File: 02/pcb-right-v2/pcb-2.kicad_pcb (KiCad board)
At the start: 2 copper layers, 146.9 x 86 mm, 44 parts, among them U1 Arduino_Pro_Micro, U2 TRRS

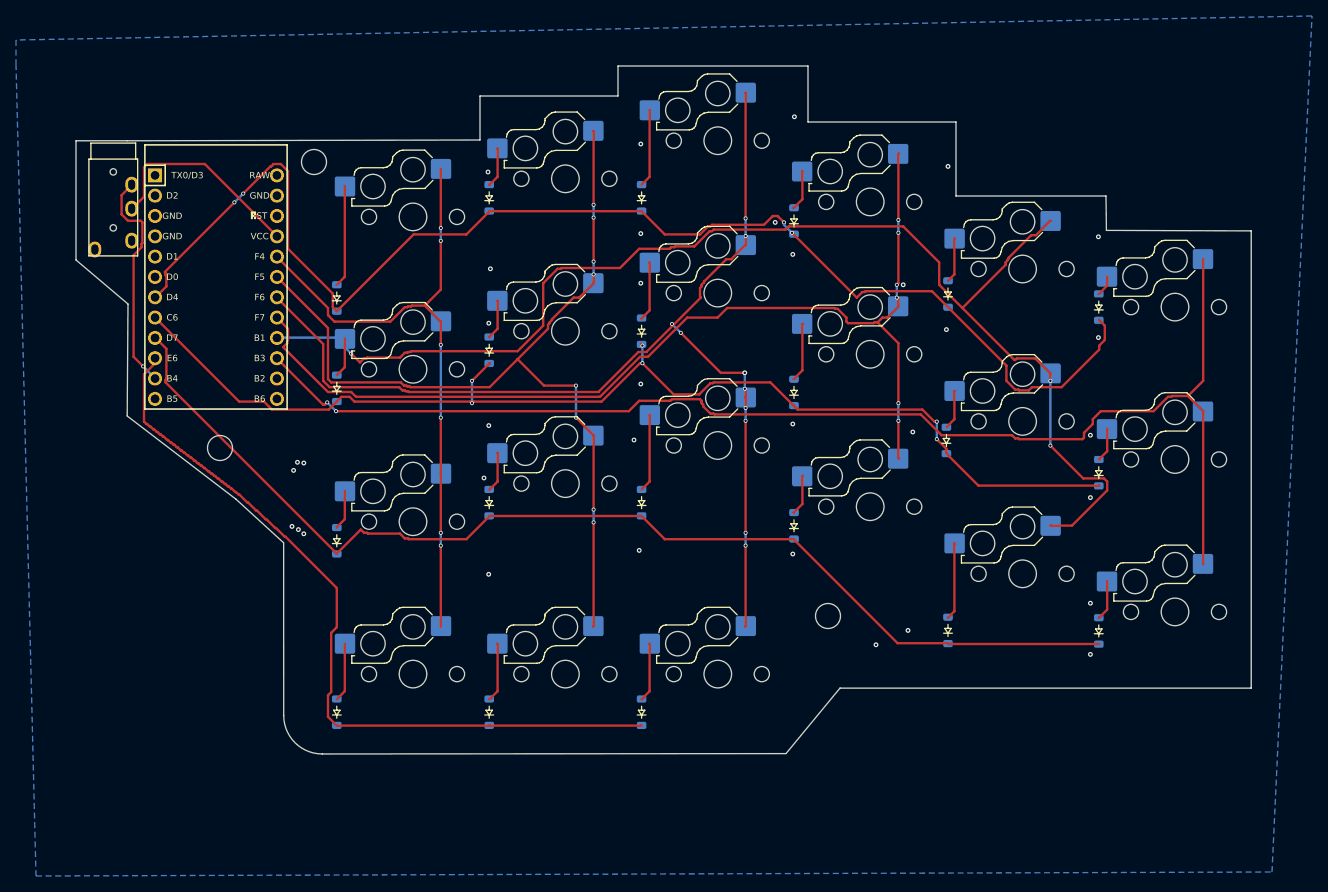
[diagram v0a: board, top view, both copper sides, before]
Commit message: fix: pcb-right-v2 switch/TRRS/MCU footprints, routing, gerbers
Switches, TRRS jack, and Pro Micro were locally mirrored (Y-flipped)
instead of repositioned, which doesn't work for real, non-mirrorable
parts — pins only go in one way regardless of which board half they're
on. Reset all three to the left board's exact pad geometry and
rotation, moved to their correct mirrored positions on the right board,
with net wiring preserved.

Re-routed after each footprint fix (rotation changes move pad
positions) and cleared a copper-to-edge-cuts clearance violation near
a mounting hole. DRC is now clean except for pre-existing,
non-blocking warnings shared with the left board.

Added production/ gerbers and drill files, matching the left board's
file set and naming convention.

Co-Authored-By: Claude Sonnet 5 <noreply@anthropic.com>
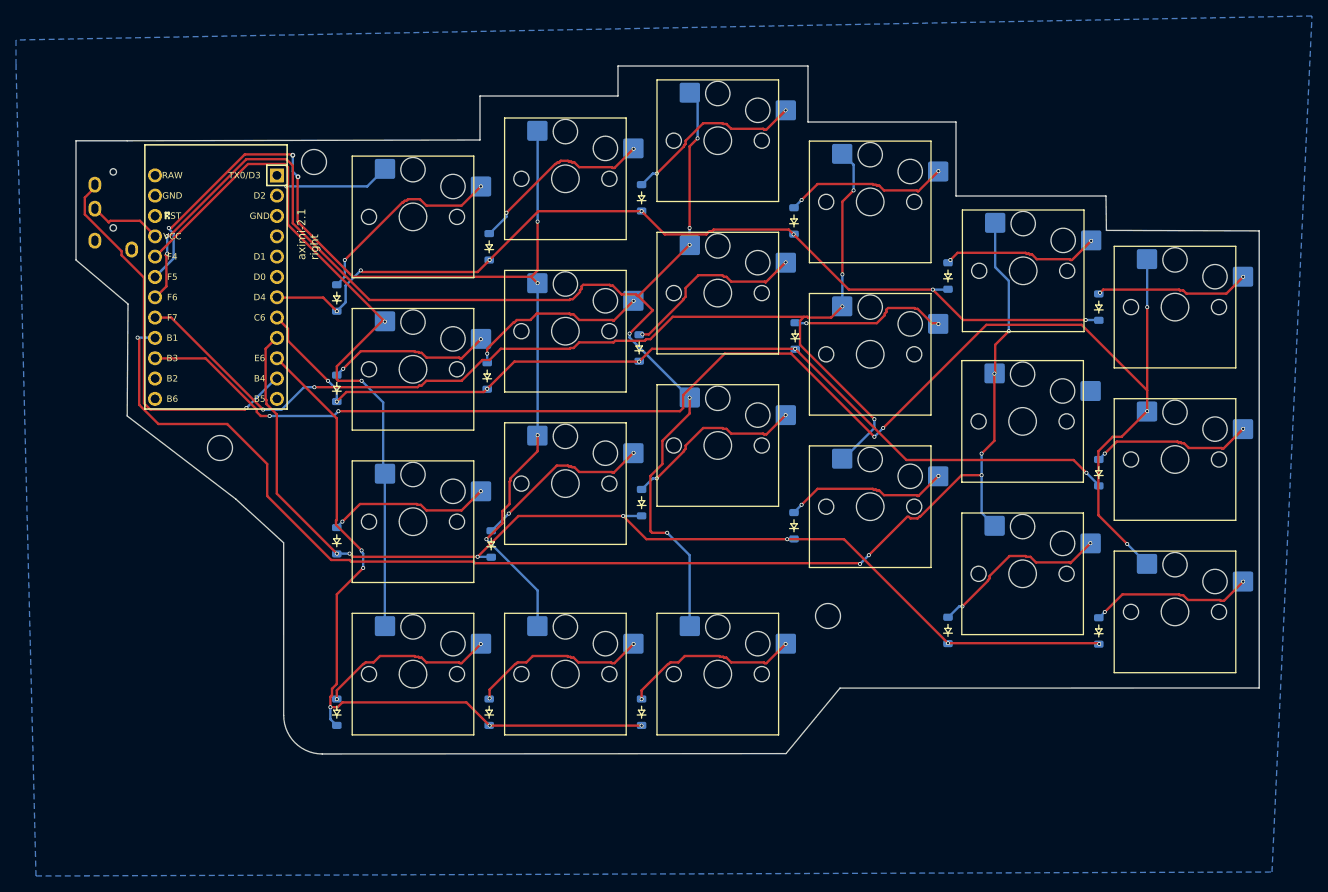
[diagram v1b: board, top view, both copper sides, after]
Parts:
- removed D8: Diode, Scotto Components:Diode_SOD-123
- moved D9 7.05 mm to (128.0, 56.0)
- moved D5 6.12 mm to (89.8, 44.9)
- moved D17 5.17 mm to (90.0, 82.0)
- moved D11 3.23 mm to (89.5, 61.0)
- moved D2 2.25 mm to (147.1, 48.5)
- moved D10 2.12 mm to (108.5, 57.5)
- moved S2 0.24 mm to (156.5, 47.9), turned to 0 degrees
- turned S1 to 0 degrees
- turned S10 to 0 degrees
- turned S11 to 0 degrees
- turned S12 to 0 degrees
- turned S13 to 0 degrees
- turned S14 to 0 degrees
- turned S15 to 0 degrees
- turned S16 to 0 degrees
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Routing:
- net Row 1: track 165.4 -> 118.2 mm, vias 4 -> 7
- net Column 4: track 137.6 -> 164.9 mm, vias 15 -> 8
- net Column 1: track 162.6 -> 188.7 mm, vias 4 -> 7
- net Row 2: track 143.6 -> 118.8 mm
- net Column 6: track 82.2 -> 104.6 mm, vias 12 -> 3
- net Column 5: track 113.8 -> 135.2 mm, vias 14 -> 7
- net TRRS Data: track 28.3 -> 49.1 mm
- net Net-(D5-A): track 5.02 -> 23.5 mm, vias 0 -> 2
- net Net-(D11-A): track 5.00 -> 23.4 mm, vias 0 -> 2
- net Net-(D17-A): track 5.12 -> 22.7 mm, vias 0 -> 2
- net Power: track 26.3 -> 9.07 mm
- net Net-(D1-A): track 2.60 -> 19.3 mm, vias 0 -> 2
- net Net-(D7-A): track 4.32 -> 20.4 mm, vias 0 -> 2
- net Net-(D10-A): track 7.51 -> 23.5 mm, vias 0 -> 2
- net Net-(D15-A): track 5.16 -> 20.8 mm, vias 0 -> 2
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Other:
- board size 146.9 x 86 mm -> 147.9 x 86 mm
- board text added: "aximi-2.1 right"
- board text removed: "aximi-2.0 right"
